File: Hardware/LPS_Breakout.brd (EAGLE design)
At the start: 11.6 x 14.2 mm, 11 parts

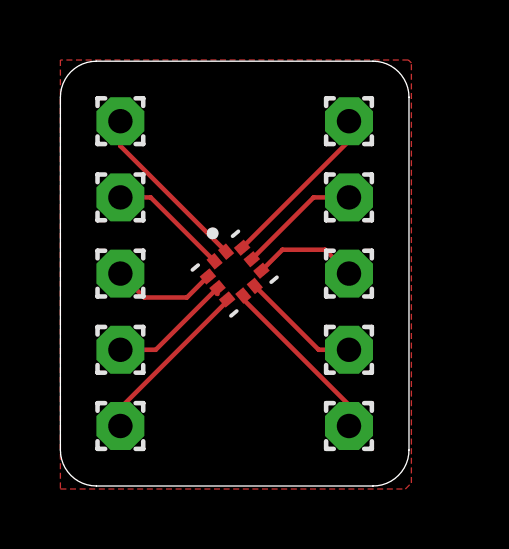
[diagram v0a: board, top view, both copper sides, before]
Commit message: updated pinheaders and names
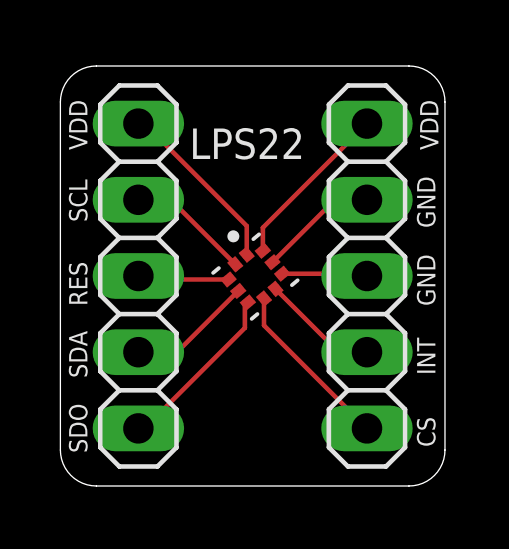
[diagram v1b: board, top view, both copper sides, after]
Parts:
- removed PAD1, PAD10, PAD2, PAD3, PAD4, PAD5, PAD6, PAD7, PAD8, PAD9: (no value), wirepad:1,6/0,8
- added JP1, JP2: (no value), pinhead:1X05
- moved A1 0.70 mm to (6.50, 6.98)
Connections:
- removed net N$7: A1.7, PAD7.1
- new net N$9: A1.8, A1.9, JP1.3, JP1.4
- net N$1: now also JP2.1; no longer PAD1.1
- net N$10: now also JP1.5; no longer PAD10.1
- net N$2: now also JP2.2; no longer PAD2.1
- net N$3: now also JP2.3; no longer PAD3.1
- net N$4: now also JP2.4; no longer PAD4.1
- net N$5: now also JP2.5; no longer PAD5.1
- net N$6: now also JP1.1; no longer PAD6.1
- net N$8: now also A1.7, JP1.2; no longer A1.8, A1.9, PAD8.1, PAD9.1
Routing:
- net N$9: track 0.00 -> 6.87 mm
- net N$7: track 4.02 -> 0.00 mm
- net N$8: track 7.63 -> 3.92 mm
- removed copper zone on layer 1, net GND
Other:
- board size 11.6 x 14.2 mm -> 12.8 x 14 mm
- board text added: "CS"
- board text added: "GND"
- board text added: "INT"
- board text added: "LPS22"
- board text added: "RES"
- board text added: "SCL"
- board text added: "SDA"
- board text added: "SDO"
- board text added: "VDD"
